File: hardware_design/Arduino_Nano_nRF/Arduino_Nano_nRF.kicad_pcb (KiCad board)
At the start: 2 copper layers, 7 parts, among them J1 Conn_02x04_Odd_Even, P1 Digital, P2 Analog, P3 CONN_01X01, P4 CONN_01X01, P5 CONN_01X01, P6 CONN_01X01

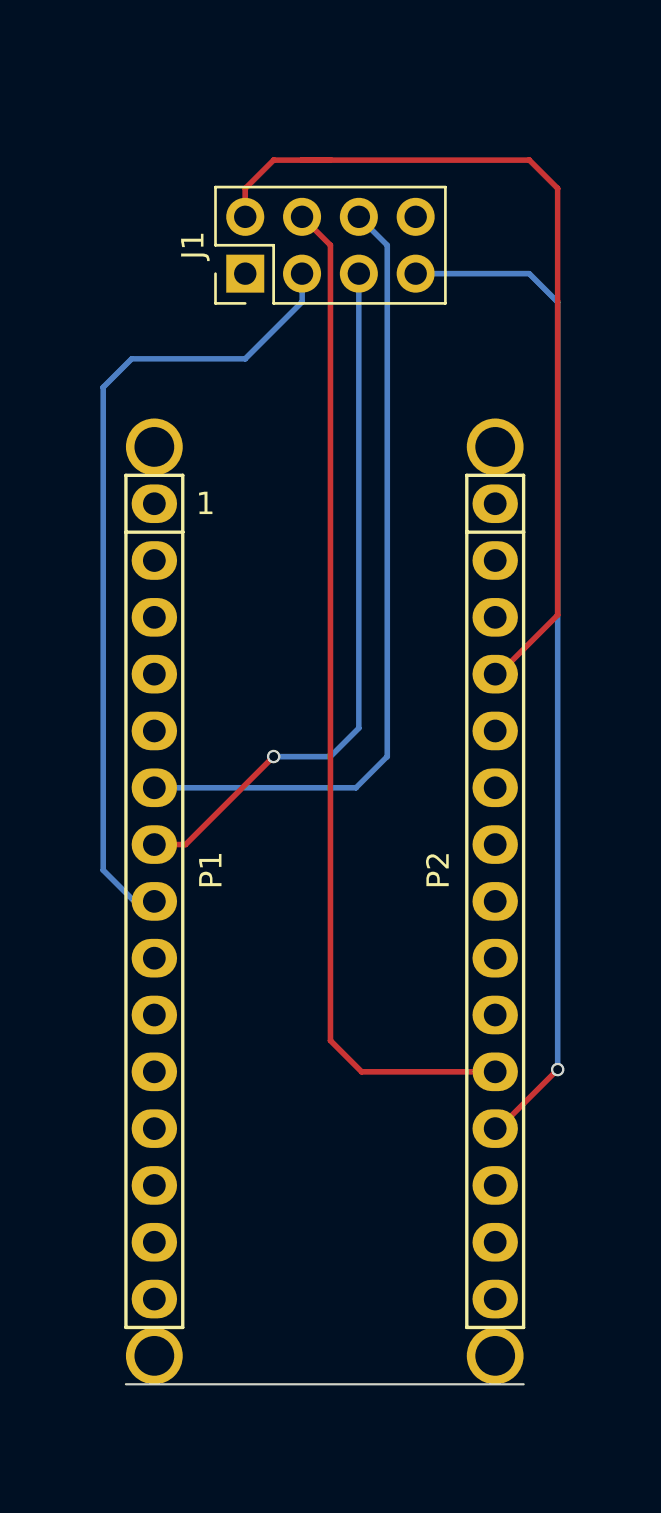
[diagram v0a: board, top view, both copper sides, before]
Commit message: Completed layout for nRF Dongle
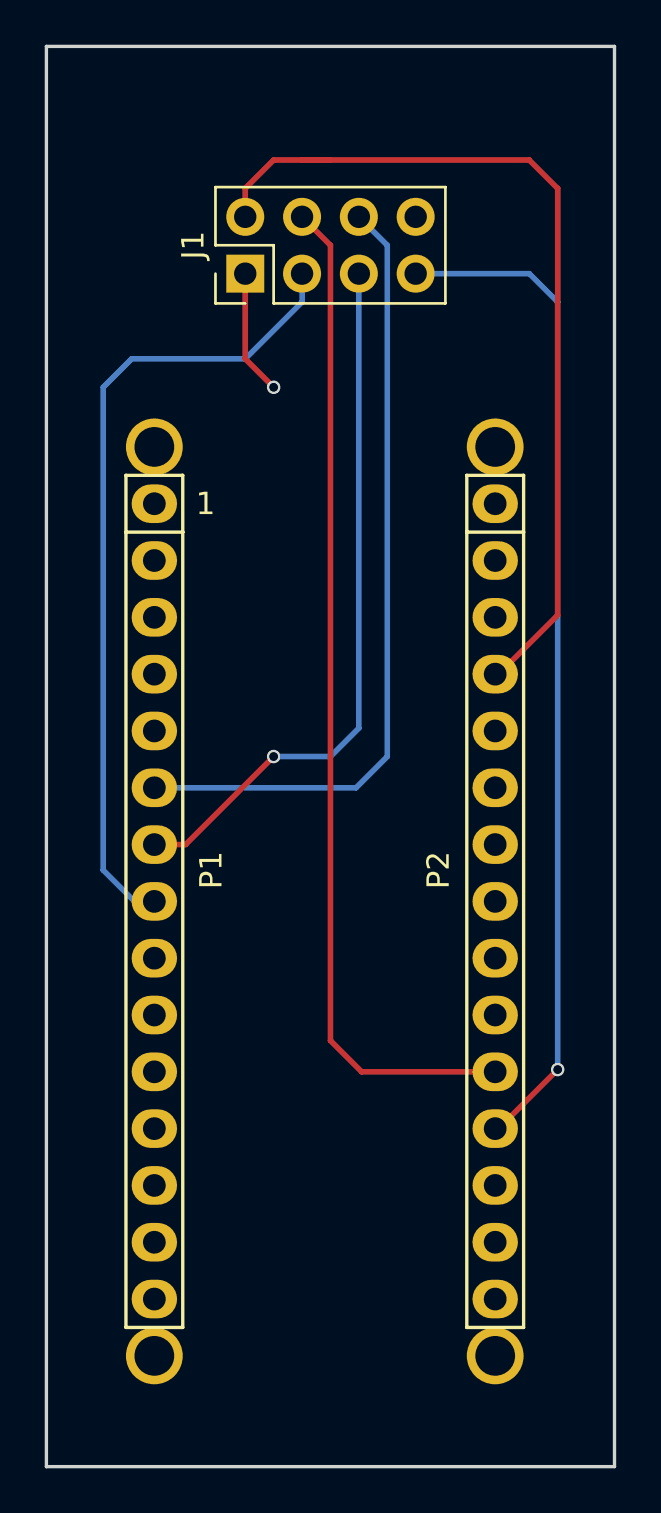
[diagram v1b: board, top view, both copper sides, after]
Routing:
- net GND: track 0.00 -> 5.61 mm, vias 0 -> 1
- added copper zone on B.Cu, net GND
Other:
- board outline added: 25.4 x 63.5 mm
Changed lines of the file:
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@@
   (general
     (thickness 1.6)
-    (drawings 17)
-    (tracks 41)
+    (drawings 20)
+    (tracks 44)
     (zones 0)
     (modules 7)
@@
     (visible_elements FFFFFF7F)
     (pcbplotparams
-      (layerselection 0x00030_80000001)
+      (layerselection 0x00030_ffffffff)
       (usegerberextensions false)
       (usegerberattributes false)
@@
       (padsonsilk false)
       (subtractmaskfromsilk false)
-      (outputformat 1)
+      (outputformat 4)
       (mirror false)
-      (drillshape 1)
+      (drillshape 0)
       (scaleselection 1)
       (outputdirectory ""))
@@
       (net 29 "Net-(P6-Pad1)"))
   )
+  (gr_line (start 134.62 114.3) (end 134.62 50.8) (layer Edge.Cuts) (width 0.15))
+  (gr_line (start 160.02 114.3) (end 134.62 114.3) (layer Edge.Cuts) (width 0.15))
+  (gr_line (start 160.02 50.8) (end 160.02 114.3) (layer Edge.Cuts) (width 0.15))
+  (gr_line (start 134.62 50.8) (end 160.02 50.8) (layer Edge.Cuts) (width 0.15))
   (gr_text 1 (at 141.732 71.247) (layer F.SilkS)
     (effects (font (size 1 1) (thickness 0.15)))
@@
   (gr_line (start 143.256 72.517) (end 150.876 72.517) (angle 90) (layer Dwgs.User) (width 0.15))
   (gr_line (start 143.256 67.437) (end 143.256 72.517) (angle 90) (layer Dwgs.User) (width 0.15))
-  (gr_line (start 138.176 110.617) (end 155.956 110.617) (angle 90) (layer Edge.Cuts) (width 0.1))
+  (segment (start 143.51 60.96) (end 143.51 64.77) (width 0.25) (layer F.Cu) (net 4))
+  (via (at 144.78 66.04) (size 0.6) (drill 0.4) (layers F.Cu B.Cu) (net 4))
+  (segment (start 143.51 64.77) (end 144.78 66.04) (width 0.25) (layer F.Cu) (net 4))
   (segment (start 148.59 58.42) (end 149.86 59.69) (width 0.25) (layer B.Cu) (net 6))
   (segment (start 149.86 59.69) (end 149.86 82.55) (width 0.25) (layer B.Cu) (net 6))
@@
   (segment (start 156.21 60.96) (end 151.13 60.96) (width 0.25) (layer B.Cu) (net 23))
   (segment (start 157.48 62.23) (end 156.21 60.96) (width 0.25) (layer B.Cu) (net 23))
+  (zone (net 4) (net_name GND) (layer B.Cu) (hatch edge 0.508)
+    (connect_pads (clearance 0.508))
+    (min_thickness 0.254)
+    (fill yes (arc_segments 16) (thermal_gap 0.508) (thermal_bridge_width 0.508))
+    (polygon
+      (pts
+        (xy 134.62 50.8) (xy 160.02 50.8) (xy 160.02 114.3) (xy 134.62 114.3)
+      )
+    )
+  )
 )
